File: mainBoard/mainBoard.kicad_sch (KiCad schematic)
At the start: 20 parts, among them J10 Conn_01x01, J11 Conn_01x01, J12 Conn_01x01, J13 Conn_01x01, J9 Conn_01x01

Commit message: ukild
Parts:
- renumbered J9 to J1, J10 to J2, J11 to J3, J12 to J4, J13 to J5, J9 to J6, J9 to J7, J9 to J8
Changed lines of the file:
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@@
     (effects (font (size 1.27 1.27)) (justify left bottom))
   )
-  (label "TUNING-LINES.SWDIO" (at 139.7 50.8 180)
+  (label "TUNING-LINES.SWDIO" (at 139.7 50.8 180) (fields_autoplaced)
     (effects (font (size 1.27 1.27)) (justify right bottom))
   )
@@
     (effects (font (size 1.27 1.27)) (justify left bottom))
   )
-  (label "TUNING-LINES.TX-2" (at 139.7 66.04 180)
+  (label "TUNING-LINES.TX-2" (at 139.7 66.04 180) (fields_autoplaced)
     (effects (font (size 1.27 1.27)) (justify right bottom))
   )
-  (label "TUNING-LINES.NRST" (at 139.7 60.96 180)
+  (label "TUNING-LINES.NRST" (at 139.7 60.96 180) (fields_autoplaced)
     (effects (font (size 1.27 1.27)) (justify right bottom))
   )
-  (label "TUNING-LINES.RX-2" (at 139.7 71.12 180)
+  (label "TUNING-LINES.RX-2" (at 139.7 71.12 180) (fields_autoplaced)
     (effects (font (size 1.27 1.27)) (justify right bottom))
   )
-  (label "TUNING-LINES.SWCLK" (at 139.7 55.88 180)
+  (label "TUNING-LINES.SWCLK" (at 139.7 55.88 180) (fields_autoplaced)
     (effects (font (size 1.27 1.27)) (justify right bottom))
   )
@@
   (symbol (lib_id "Connector_Generic:Conn_01x01") (at 144.78 96.52 0) (mirror x) (unit 1)
     (in_bom yes) (on_board yes) (dnp no)
-    (property "Reference" "J9" (at 148.59 96.52 0)
+    (property "Reference" "J6" (at 148.59 96.52 0)
       (effects (font (size 1.27 1.27)))
     )
@@
   (symbol (lib_id "Connector_Generic:Conn_01x01") (at 160.02 71.12 180) (unit 1)
     (in_bom yes) (on_board yes) (dnp no)
-    (property "Reference" "J13" (at 156.21 71.12 0)
+    (property "Reference" "J5" (at 156.21 71.12 0)
       (effects (font (size 1.27 1.27)))
     )
@@
   (symbol (lib_id "Connector_Generic:Conn_01x01") (at 144.78 66.04 0) (mirror x) (unit 1)
     (in_bom yes) (on_board yes) (dnp no)
-    (property "Reference" "J12" (at 148.59 66.04 0)
+    (property "Reference" "J4" (at 148.59 66.04 0)
       (effects (font (size 1.27 1.27)))
     )
@@
   (symbol (lib_id "Connector_Generic:Conn_01x01") (at 160.02 93.98 180) (unit 1)
     (in_bom yes) (on_board yes) (dnp no)
-    (property "Reference" "J9" (at 156.21 93.98 0)
+    (property "Reference" "J7" (at 156.21 93.98 0)
       (effects (font (size 1.27 1.27)))
     )
@@
   (symbol (lib_id "Connector_Generic:Conn_01x01") (at 160.02 99.06 0) (mirror y) (unit 1)
     (in_bom yes) (on_board yes) (dnp no)
-    (property "Reference" "J9" (at 156.21 99.06 0)
+    (property "Reference" "J8" (at 156.21 99.06 0)
       (effects (font (size 1.27 1.27)))
     )
@@
   (symbol (lib_id "Connector_Generic:Conn_01x01") (at 160.02 55.88 180) (unit 1)
     (in_bom yes) (on_board yes) (dnp no)
-    (property "Reference" "J10" (at 156.21 55.88 0)
+    (property "Reference" "J2" (at 156.21 55.88 0)
       (effects (font (size 1.27 1.27)))
     )
@@
   (symbol (lib_id "Connector_Generic:Conn_01x01") (at 144.78 60.96 0) (mirror x) (unit 1)
     (in_bom yes) (on_board yes) (dnp no)
-    (property "Reference" "J11" (at 148.59 60.96 0)
+    (property "Reference" "J3" (at 148.59 60.96 0)
       (effects (font (size 1.27 1.27)))
     )
@@
   (symbol (lib_id "Connector_Generic:Conn_01x01") (at 160.02 66.04 180) (unit 1)
     (in_bom yes) (on_board yes) (dnp no)
-    (property "Reference" "J12" (at 156.21 66.04 0)
+    (property "Reference" "J4" (at 156.21 66.04 0)
       (effects (font (size 1.27 1.27)))
     )
@@
   (symbol (lib_id "Connector_Generic:Conn_01x01") (at 144.78 50.8 0) (mirror x) (unit 1)
     (in_bom yes) (on_board yes) (dnp no)
-    (property "Reference" "J9" (at 148.59 50.8 0)
+    (property "Reference" "J1" (at 148.59 50.8 0)
       (effects (font (size 1.27 1.27)))
     )
@@
   (symbol (lib_id "Connector_Generic:Conn_01x01") (at 144.78 71.12 0) (mirror x) (unit 1)
     (in_bom yes) (on_board yes) (dnp no)
-    (property "Reference" "J13" (at 148.59 71.12 0)
+    (property "Reference" "J5" (at 148.59 71.12 0)
       (effects (font (size 1.27 1.27)))
     )
@@
   (symbol (lib_id "Connector_Generic:Conn_01x01") (at 144.78 99.06 0) (unit 1)
     (in_bom yes) (on_board yes) (dnp no)
-    (property "Reference" "J9" (at 148.59 99.06 0)
+    (property "Reference" "J8" (at 148.59 99.06 0)
       (effects (font (size 1.27 1.27)))
     )
@@
   (symbol (lib_id "Connector_Generic:Conn_01x01") (at 160.02 60.96 180) (unit 1)
     (in_bom yes) (on_board yes) (dnp no)
-    (property "Reference" "J11" (at 156.21 60.96 0)
+    (property "Reference" "J3" (at 156.21 60.96 0)
       (effects (font (size 1.27 1.27)))
     )
@@
   (symbol (lib_id "Connector_Generic:Conn_01x01") (at 160.02 96.52 180) (unit 1)
     (in_bom yes) (on_board yes) (dnp no)
-    (property "Reference" "J9" (at 156.21 96.52 0)
+    (property "Reference" "J6" (at 156.21 96.52 0)
       (effects (font (size 1.27 1.27)))
     )
@@
   (symbol (lib_id "Connector_Generic:Conn_01x01") (at 144.78 55.88 0) (mirror x) (unit 1)
     (in_bom yes) (on_board yes) (dnp no)
-    (property "Reference" "J10" (at 148.59 55.88 0)
+    (property "Reference" "J2" (at 148.59 55.88 0)
       (effects (font (size 1.27 1.27)))
     )
@@
   (symbol (lib_id "Connector_Generic:Conn_01x01") (at 144.78 93.98 0) (mirror x) (unit 1)
     (in_bom yes) (on_board yes) (dnp no)
-    (property "Reference" "J9" (at 148.59 93.98 0)
+    (property "Reference" "J7" (at 148.59 93.98 0)
       (effects (font (size 1.27 1.27)))
     )
@@
   (symbol (lib_id "Connector_Generic:Conn_01x01") (at 160.02 50.8 180) (unit 1)
     (in_bom yes) (on_board yes) (dnp no)
-    (property "Reference" "J9" (at 156.21 50.8 0)
-      (effects (font (size 1.27 1.27)))
-    )
+    (property "Reference" "J1" (at 156.21 50.8 0)
+      (effects (font (size 1.27 1.27)))
+    )

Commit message: DebugBoard
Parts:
- renumbered J9 to J12, J1 to J13, J2 to J14, J3 to J15, J4 to J16, J5 to J17, J7 to J18, J6 to J19, J8 to J20, J9 to J21, J9 to J22
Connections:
- net DebuBoard/GND: now reaches J22.1 (Pin_1)
- net DB-DRV.PROUD renamed DB-DRV.CURRENT
- net DB-DRV.VREF renamed DB-TUNING-LINES.TRACESWO
- net DRV.PROUD renamed DRV.CURRENT
- net DRV.VREF renamed TUNING-LINES.TRACESWO
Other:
- sheet DebuBoard ports: added DB-DRV{IN1 IN2 VREF CURRENT}, DB-TUNING-LINES{TX-2 RX-2 SWDIO SWCLK NRST TRACESWO}, GND; removed DB-DRV{IN1 IN2 VREF PROUD}, DB-TUNING-LINES{TX-2 RX-2 SWDIO SWCLK NRST}
- sheet MotorBoard ports: added DRV{IN1 IN2 VREF CURRENT}, TUNING-LINES{TX-2 RX-2 SWDIO SWCLK NRST TRACESWO}; removed DRV{IN1 IN2 VREF PROUD}, TUNING-LINES{TX-2 RX-2 SWDIO SWCLK NRST}
- moved on the sheet: J1, J12, J13, J14, J15, J16, J17, J18, J19, J2, J20, J21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

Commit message: Add LCSC code
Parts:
- J1, J12, J2, J3, J4, J5, J6, J7, J8, J9: JLCPCB_IGNORE (none) -> 1
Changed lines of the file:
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@@
+      (effects (font (size 1.27 1.27)) hide)
+    )
+    (property "JLCPCB_IGNORE" "1" (at 138.43 96.52 0)
       (effects (font (size 1.27 1.27)) hide)
     )
@@
       (effects (font (size 1.27 1.27)) hide)
     )
+    (property "JLCPCB_IGNORE" "1" (at 138.43 63.5 0)
+      (effects (font (size 1.27 1.27)) hide)
+    )
     (pin "1")
     (instances
@@
       (effects (font (size 1.27 1.27)) hide)
     )
+    (property "JLCPCB_IGNORE" "1" (at 138.43 104.14 0)
+      (effects (font (size 1.27 1.27)) hide)
+    )
     (pin "1")
     (instances
@@
       (effects (font (size 1.27 1.27)) hide)
     )
+    (property "JLCPCB_IGNORE" "1" (at 138.43 58.42 0)
+      (effects (font (size 1.27 1.27)) hide)
+    )
     (pin "1")
     (instances
@@
       (effects (font (size 1.27 1.27)) hide)
     )
+    (property "JLCPCB_IGNORE" "1" (at 138.43 48.26 0)
+      (effects (font (size 1.27 1.27)) hide)
+    )
     (pin "1")
     (instances
@@
       (effects (font (size 1.27 1.27)) hide)
     )
+    (property "JLCPCB_IGNORE" "1" (at 138.43 111.76 0)
+      (effects (font (size 1.27 1.27)) hide)
+    )
     (pin "1")
     (instances
@@
       (effects (font (size 1.27 1.27)) hide)
     )
+    (property "JLCPCB_IGNORE" "1" (at 138.43 68.58 0)
+      (effects (font (size 1.27 1.27)) hide)
+    )
     (pin "1")
     (instances
@@
       (effects (font (size 1.27 1.27)) hide)
     )
+    (property "JLCPCB_IGNORE" "1" (at 138.43 73.66 0)
+      (effects (font (size 1.27 1.27)) hide)
+    )
     (pin "1")
     (instances
@@
       (effects (font (size 1.27 1.27)) hide)
     )
+    (property "JLCPCB_IGNORE" "1" (at 138.43 53.34 0)
+      (effects (font (size 1.27 1.27)) hide)
+    )
     (pin "1")
     (instances
@@
       (effects (font (size 1.27 1.27)) hide)
     )
+    (property "JLCPCB_IGNORE" "1" (at 138.43 93.98 0)
+      (effects (font (size 1.27 1.27)) hide)
+    )

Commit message: LCSC cods
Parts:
- J13, J14, J15, J16, J17, J18, J19, J20, J21, J22: LCSC (none) -> C5157325
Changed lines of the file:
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@@
+      (effects (font (size 1.27 1.27)) hide)
+    )
+    (property "LCSC" "C5157325" (at 153.67 111.76 0)
       (effects (font (size 1.27 1.27)) hide)
     )
@@
       (effects (font (size 1.27 1.27)) hide)
     )
+    (property "LCSC" "C5157325" (at 153.67 68.58 0)
+      (effects (font (size 1.27 1.27)) hide)
+    )
     (pin "1")
     (instances
@@
       (effects (font (size 1.27 1.27)) hide)
     )
+    (property "LCSC" "C5157325" (at 153.67 93.98 0)
+      (effects (font (size 1.27 1.27)) hide)
+    )
     (pin "1")
     (instances
@@
       (effects (font (size 1.27 1.27)) hide)
     )
+    (property "LCSC" "C5157325" (at 153.67 73.66 0)
+      (effects (font (size 1.27 1.27)) hide)
+    )
     (pin "1")
     (instances
@@
       (effects (font (size 1.27 1.27)) hide)
     )
+    (property "LCSC" "C5157325" (at 153.67 53.34 0)
+      (effects (font (size 1.27 1.27)) hide)
+    )
     (pin "1")
     (instances
@@
       (effects (font (size 1.27 1.27)) hide)
     )
+    (property "LCSC" "C5157325" (at 153.67 63.5 0)
+      (effects (font (size 1.27 1.27)) hide)
+    )
     (pin "1")
     (instances
@@
       (effects (font (size 1.27 1.27)) hide)
     )
+    (property "LCSC" "C5157325" (at 153.67 104.14 0)
+      (effects (font (size 1.27 1.27)) hide)
+    )
     (pin "1")
     (instances
@@
       (effects (font (size 1.27 1.27)) hide)
     )
+    (property "LCSC" "C5157325" (at 153.67 58.42 0)
+      (effects (font (size 1.27 1.27)) hide)
+    )
     (pin "1")
     (instances
@@
       (effects (font (size 1.27 1.27)) hide)
     )
+    (property "LCSC" "C5157325" (at 153.67 96.52 0)
+      (effects (font (size 1.27 1.27)) hide)
+    )
     (pin "1")
     (instances
@@
       (effects (font (size 1.27 1.27)) hide)
     )
+    (property "LCSC" "C5157325" (at 153.67 48.26 0)
+      (effects (font (size 1.27 1.27)) hide)
+    )

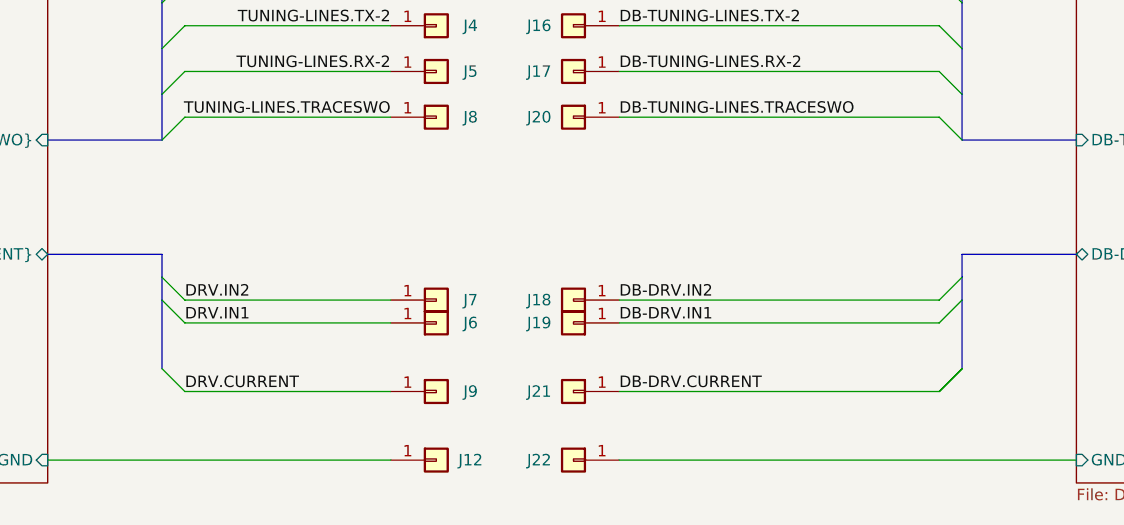
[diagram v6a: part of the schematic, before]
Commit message: Increasing motor pedals
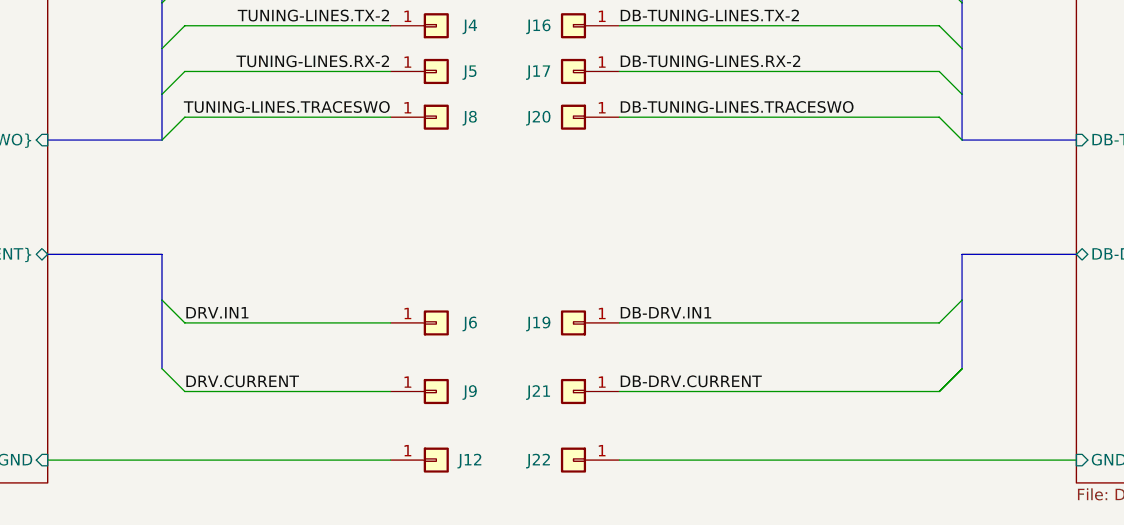
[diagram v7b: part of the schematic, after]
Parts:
- removed J18: Conn_01x01, RKL-Connectors:YZ157015035P-01, symbol Connector_Generic:Conn_01x01
- removed J7: Conn_01x01, RKL-Connectors:YZ157015035P-01-contact_pad, symbol Connector_Generic:Conn_01x01
